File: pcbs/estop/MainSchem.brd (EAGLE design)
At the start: 99 x 99.5 mm, 30 parts, among them J1 XT60-M, J2 XT60-M, J3 XT60-M, J4 XT60-M, J5 XT60-M, Q1 FDBL9401-F085, Q2 FDBL9401-F085, U1 FAN3100T, U2 FAN3100T

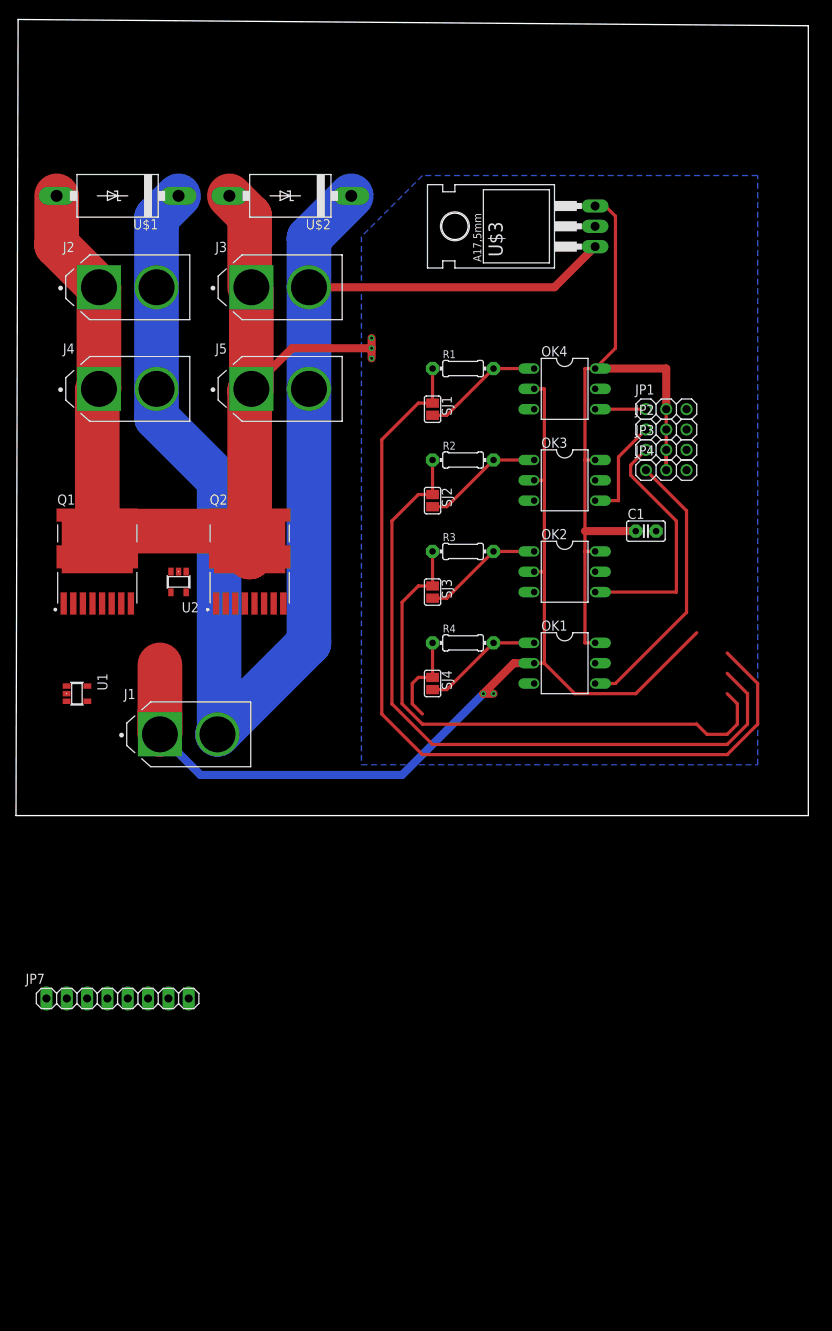
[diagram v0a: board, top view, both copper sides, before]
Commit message: Made improvements to e-stop layout and schematic. Added high-current pads.
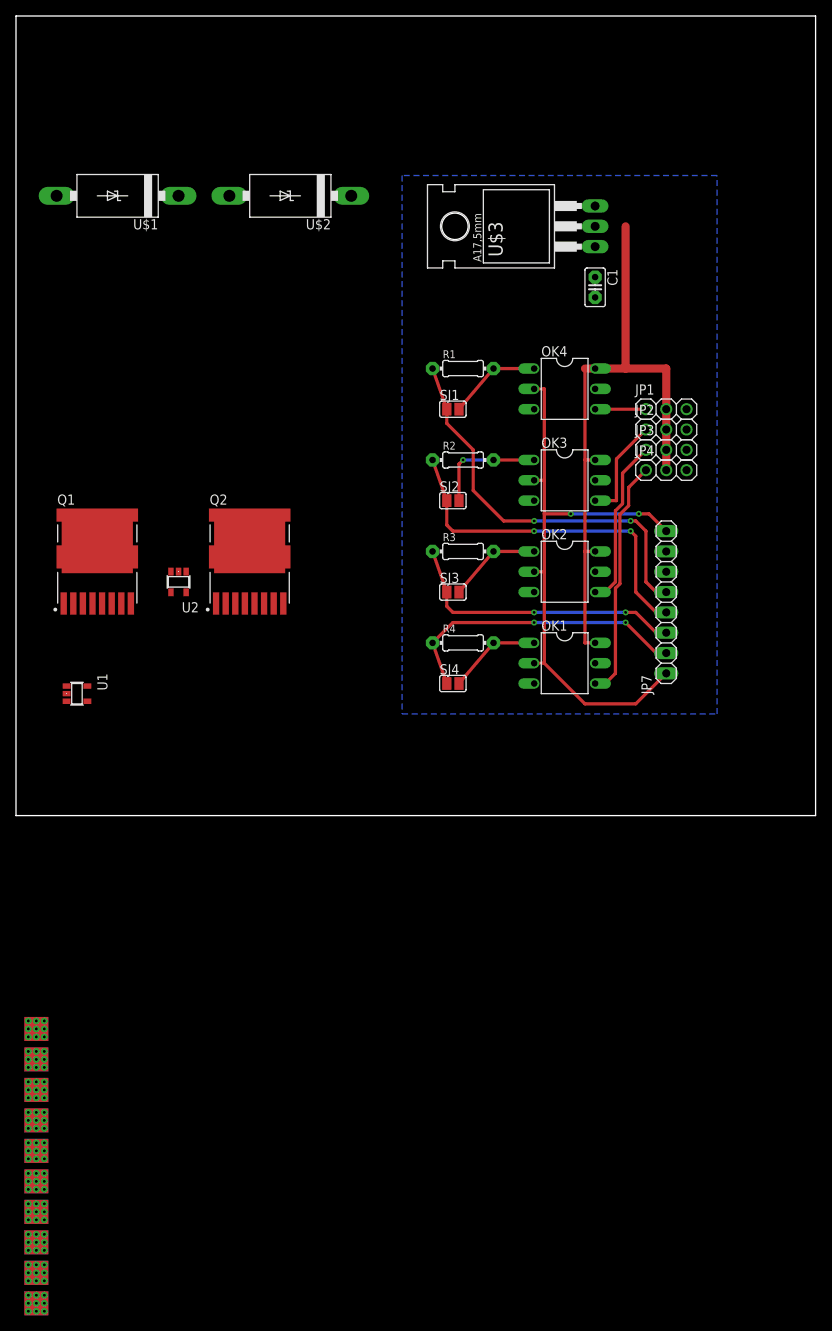
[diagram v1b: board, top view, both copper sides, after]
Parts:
- removed J1, J2, J3, J4, J5: XT60-M, XT60-M:AMASS_XT60-M
- added U$10, U$11, U$12, U$13, U$4, U$5, U$6, U$7, U$8, U$9: HIGH_CURRENT_WIRE_PAD, HighCurrentTransistorAndDriver:HIGH_CURRENT_WIRE_PAD
- moved JP7 84.6 mm to (81.3, 26.7), turned to 90 degrees
- moved C1 31.1 mm to (72.4, 66.0), turned to 270 degrees
- moved SJ1 2.54 mm to (54.6, 50.8), turned to 0 degrees
- moved SJ2 2.54 mm to (54.6, 39.4), turned to 0 degrees
- moved SJ3 2.54 mm to (54.6, 27.9), turned to 0 degrees
- moved SJ4 2.54 mm to (54.6, 16.5), turned to 0 degrees
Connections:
- net N$8 renamed ESTOP_LOW
- removed net BAT+: J1.2, J2.2, J3.2, J4.2, J5.2, JP7.7, U$1.C, U$2.C, U$3.1, U1.1, U2.1
- removed net ESC_GND: C1.2, J2.1, J3.1, J4.1, J5.1, JP1.3, JP2.3, JP3.3, JP4.3, OK1.5, OK2.5, OK3.5, OK4.5, Q1.9_1, Q1.9_2, Q1.9_3, Q1.9_4, Q2.9_1, Q2.9_2, Q2.9_3, Q2.9_4, U$1.A, U$2.A, U$3.2
- removed net ESC_SIDE_5V: C1.1, JP1.2, JP2.2, JP3.2, JP4.2, OK1.6, OK2.6, OK3.6, OK4.6, U$3.3
- removed net TRUE_GND_BATT-: J1.1, JP7.1, JP7.8, OK1.2, OK2.2, OK3.2, OK4.2, Q1.2, Q1.3, Q1.4, Q1.5, Q1.6, Q1.7, Q1.8, Q2.2, Q2.3, Q2.4, Q2.5, Q2.6, Q2.7, Q2.8, U1.2, U1.4, U2.2, U2.4
- new net +V: C1.1, JP1.2, JP2.2, JP3.2, JP4.2, JP7.7, OK1.6, OK2.6, OK3.6, OK4.6, U$1.C, U$10.P$1, U$10.P$2, U$10.P$3, U$10.P$4, U$10.P$5, U$10.P$6, U$10.P$7, U$10.P$8, U$10.P$9, U$12.P$1, U$12.P$2, U$12.P$3, U$12.P$4, U$12.P$5, U$12.P$6, U$12.P$7, U$12.P$8, U$12.P$9, U$2.C, U$3.1, U$3.3, U$4.P$1, U$4.P$2, U$4.P$3, U$4.P$4, U$4.P$5, U$4.P$6, U$4.P$7, U$4.P$8, U$4.P$9, U$6.P$1, U$6.P$2, U$6.P$3, U$6.P$4, U$6.P$5, U$6.P$6, U$6.P$7, U$6.P$8, U$6.P$9, U$8.P$1, U$8.P$2, U$8.P$3, U$8.P$4, U$8.P$5, U$8.P$6, U$8.P$7, U$8.P$8, U$8.P$9, U1.1, U2.1
- new net EGND: JP7.1, JP7.8, OK1.2, OK2.2, OK3.2, OK4.2, Q1.2, Q1.3, Q1.4, Q1.5, Q1.6, Q1.7, Q1.8, Q2.2, Q2.3, Q2.4, Q2.5, Q2.6, Q2.7, Q2.8, U$13.P$1, U$13.P$2, U$13.P$3, U$13.P$4, U$13.P$5, U$13.P$6, U$13.P$7, U$13.P$8, U$13.P$9, U1.2, U1.4, U2.2, U2.4
- new net VSS: C1.2, JP1.3, JP2.3, JP3.3, JP4.3, OK1.5, OK2.5, OK3.5, OK4.5, Q1.9_1, Q1.9_2, Q1.9_3, Q1.9_4, Q2.9_1, Q2.9_2, Q2.9_3, Q2.9_4, U$1.A, U$11.P$1, U$11.P$2, U$11.P$3, U$11.P$4, U$11.P$5, U$11.P$6, U$11.P$7, U$11.P$8, U$11.P$9, U$2.A, U$3.2, U$5.P$1, U$5.P$2, U$5.P$3, U$5.P$4, U$5.P$5, U$5.P$6, U$5.P$7, U$5.P$8, U$5.P$9, U$7.P$1, U$7.P$2, U$7.P$3, U$7.P$4, U$7.P$5, U$7.P$6, U$7.P$7, U$7.P$8, U$7.P$9, U$9.P$1, U$9.P$2, U$9.P$3, U$9.P$4, U$9.P$5, U$9.P$6, U$9.P$7, U$9.P$8, U$9.P$9
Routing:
- net BAT+: track 185.2 -> 0.00 mm
- net ESC_GND: track 141.0 -> 0.00 mm, vias 3 -> 0
- net TRUE_GND_BATT-: track 130.5 -> 0.00 mm, vias 2 -> 0
- net ESC_SIDE_5V: track 93.0 -> 0.00 mm
- net +V: track 0.00 -> 78.7 mm
- net EGND: track 0.00 -> 74.4 mm, vias 0 -> 2
- net N$20: track 108.0 -> 50.0 mm, vias 0 -> 2
- net N$18: track 88.6 -> 44.5 mm, vias 0 -> 2
- net N$15: track 70.0 -> 36.0 mm, vias 0 -> 2
- net N$10: track 11.5 -> 37.2 mm, vias 0 -> 2
- net N$11: track 31.1 -> 21.2 mm
- net N$9: track 35.0 -> 30.0 mm
- net N$5: track 15.1 -> 11.7 mm
- net N$16: track 15.1 -> 11.7 mm
- net N$19: track 15.1 -> 11.7 mm
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- added copper zone on layer 16, net VSS
- removed copper zone on layer 16, net ESC_GND
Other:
- board size 99 x 99.5 mm -> 99.9 x 99.9 mm

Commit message: E-stop board layout appears complete.
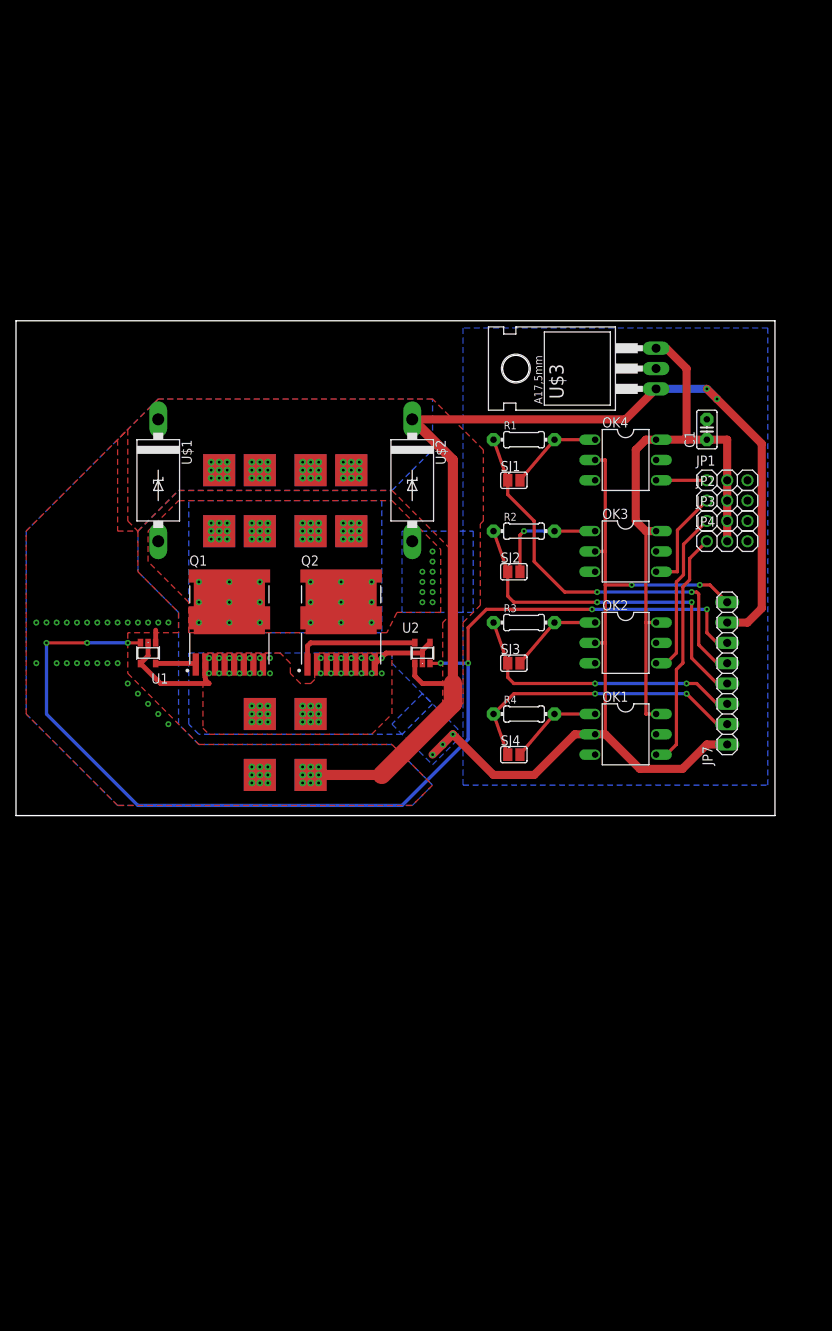
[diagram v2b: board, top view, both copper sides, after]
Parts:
- added U$14, U$15: HIGH_CURRENT_WIRE_PAD, HighCurrentTransistorAndDriver:HIGH_CURRENT_WIRE_PAD
- moved U$10 98.8 mm to (36.8, 43.2), flipped to the bottom, turned to 270 degrees
- moved U$11 97.2 mm to (41.9, 35.6), flipped to the bottom, turned to 270 degrees
- moved U$8 88.1 mm to (25.4, 43.2), flipped to the bottom, turned to 270 degrees
- moved U$9 85.9 mm to (30.5, 35.6), flipped to the bottom, turned to 270 degrees
- moved U$6 82.4 mm to (30.5, 43.2)
- moved U$4 80.2 mm to (41.9, 43.2)
- moved U$13 78.8 mm to (30.5, 12.7), flipped to the bottom, turned to 270 degrees
- moved U$7 77.1 mm to (25.4, 35.6), flipped to the bottom, turned to 270 degrees
- moved U$5 74.4 mm to (36.8, 35.6)
- moved U$12 68.2 mm to (30.5, 5.08), flipped to the bottom, turned to 270 degrees
- moved U$2 38.7 mm to (49.5, 41.9), turned to 270 degrees
- moved U$1 35.9 mm to (17.8, 41.9), turned to 270 degrees
- moved U2 31.8 mm to (50.8, 20.3), turned to 0 degrees
- moved C1 22.6 mm to (86.4, 48.3), turned to 90 degrees
- moved U$3 19.3 mm to (73.7, 55.9)
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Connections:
- removed net +V: C1.1, JP1.2, JP2.2, JP3.2, JP4.2, JP7.7, OK1.6, OK2.6, OK3.6, OK4.6, U$1.C, U$10.P$1, U$10.P$2, U$10.P$3, U$10.P$4, U$10.P$5, U$10.P$6, U$10.P$7, U$10.P$8, U$10.P$9, U$12.P$1, U$12.P$2, U$12.P$3, U$12.P$4, U$12.P$5, U$12.P$6, U$12.P$7, U$12.P$8, U$12.P$9, U$2.C, U$3.1, U$3.3, U$4.P$1, U$4.P$2, U$4.P$3, U$4.P$4, U$4.P$5, U$4.P$6, U$4.P$7, U$4.P$8, U$4.P$9, U$6.P$1, U$6.P$2, U$6.P$3, U$6.P$4, U$6.P$5, U$6.P$6, U$6.P$7, U$6.P$8, U$6.P$9, U$8.P$1, U$8.P$2, U$8.P$3, U$8.P$4, U$8.P$5, U$8.P$6, U$8.P$7, U$8.P$8, U$8.P$9, U1.1, U2.1
- new net +5V: C1.1, JP1.2, JP2.2, JP3.2, JP4.2, OK1.6, OK2.6, OK3.6, OK4.6, U$3.3
- new net V+: JP7.7, U$1.C, U$10.P$1, U$10.P$2, U$10.P$3, U$10.P$4, U$10.P$5, U$10.P$6, U$10.P$7, U$10.P$8, U$10.P$9, U$12.P$1, U$12.P$2, U$12.P$3, U$12.P$4, U$12.P$5, U$12.P$6, U$12.P$7, U$12.P$8, U$12.P$9, U$15.P$1, U$15.P$2, U$15.P$3, U$15.P$4, U$15.P$5, U$15.P$6, U$15.P$7, U$15.P$8, U$15.P$9, U$2.C, U$3.1, U$4.P$1, U$4.P$2, U$4.P$3, U$4.P$4, U$4.P$5, U$4.P$6, U$4.P$7, U$4.P$8, U$4.P$9, U$6.P$1, U$6.P$2, U$6.P$3, U$6.P$4, U$6.P$5, U$6.P$6, U$6.P$7, U$6.P$8, U$6.P$9, U$8.P$1, U$8.P$2, U$8.P$3, U$8.P$4, U$8.P$5, U$8.P$6, U$8.P$7, U$8.P$8, U$8.P$9, U1.1, U2.1
- net EGND: now also U$14.P$1, U$14.P$2, U$14.P$3, U$14.P$4, U$14.P$5, U$14.P$6, U$14.P$7, U$14.P$8, U$14.P$9
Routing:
- net V+: track 0.00 -> 143.0 mm, vias 0 -> 29
- net ESTOP_LOW: track 0.00 -> 137.0 mm, vias 0 -> 7
- net +V: track 78.7 -> 0.00 mm
- net +5V: track 0.00 -> 75.8 mm
- net EGND: track 74.4 -> 124.1 mm, vias 2 -> 33
- net N$4: track 0.00 -> 15.9 mm
- net N$6: track 0.00 -> 5.06 mm
- added copper zone on layer 1, net EGND
- added copper zone on layer 16, net EGND
- added copper zone on layer 1, net V+
- added copper zone on layer 16, net V+
- added copper zone on layer 1, net VSS
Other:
- board size 99.9 x 99.9 mm -> 94.9 x 61.8 mm

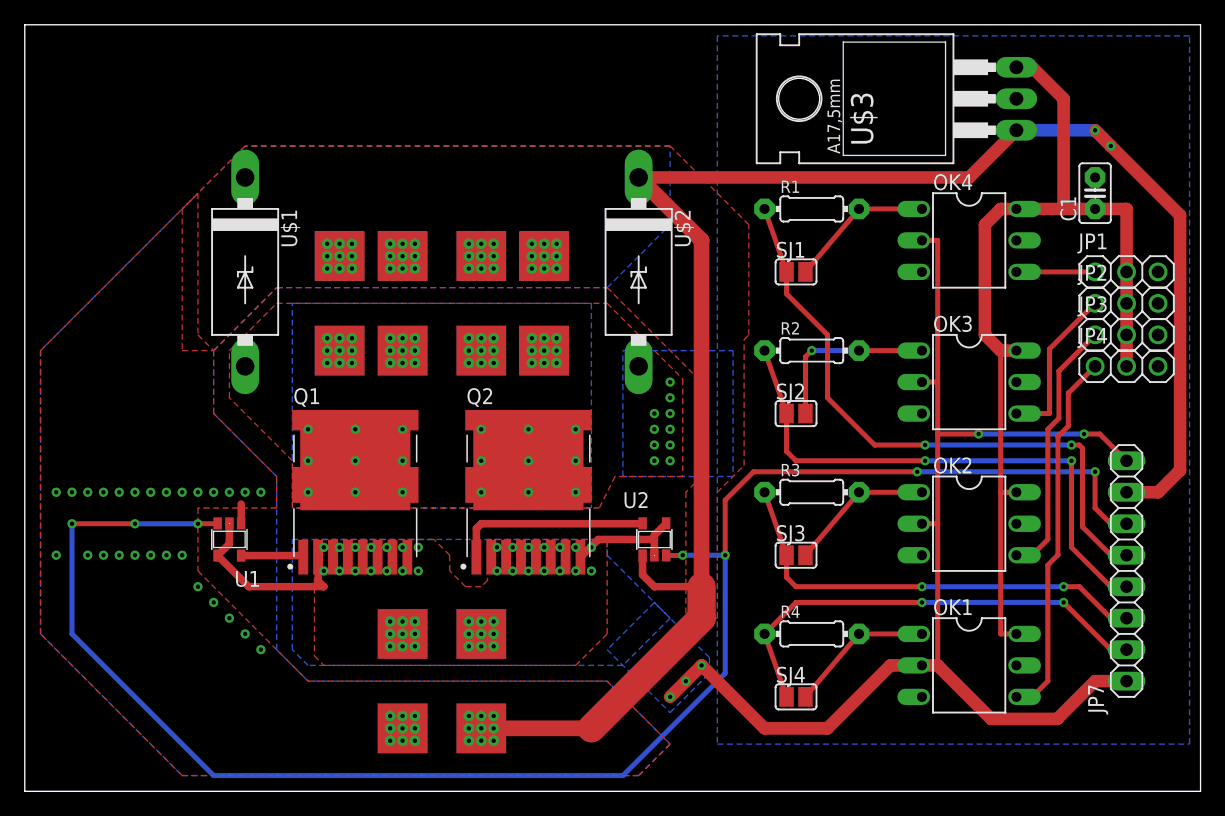
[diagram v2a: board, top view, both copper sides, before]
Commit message: Imported RPi mounting holes from one of my previous projects. Added RPi-compatible mounting holes to E-stop board.
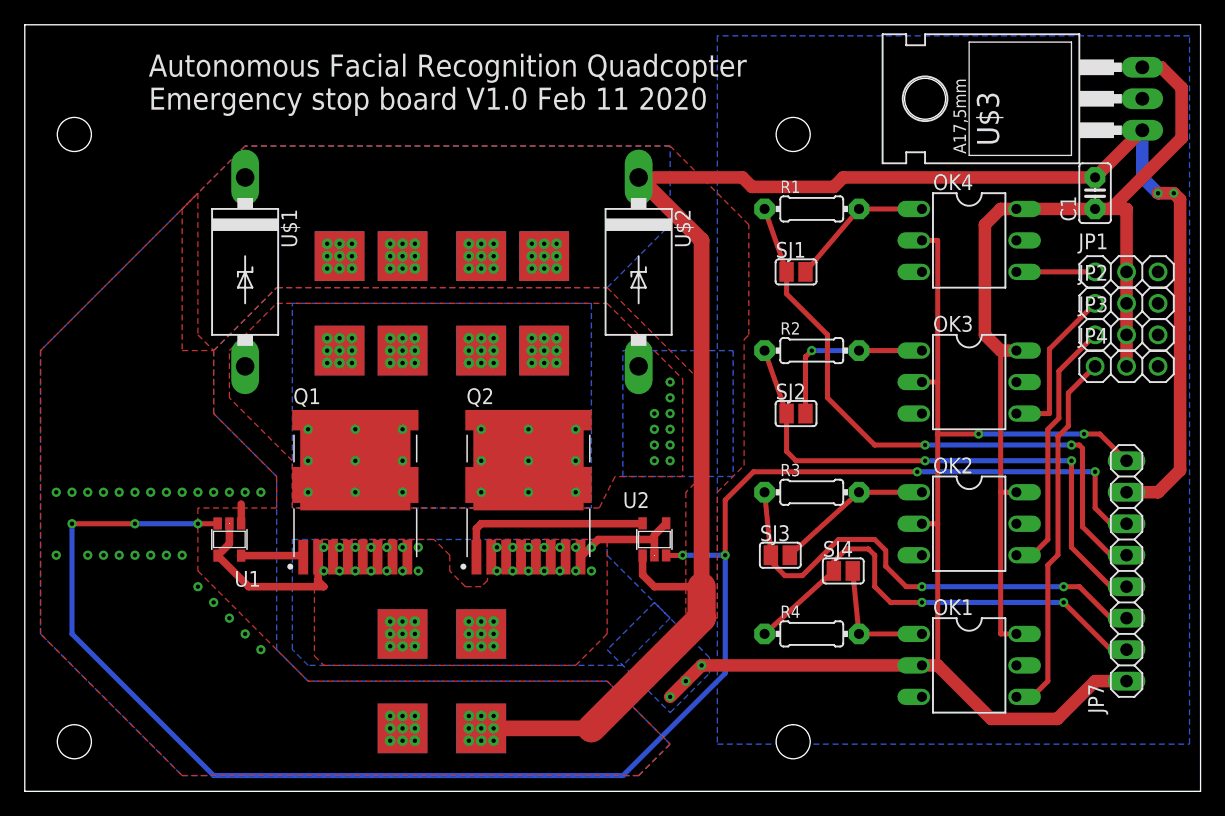
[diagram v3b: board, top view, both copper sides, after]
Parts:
- added U$16, U$17, U$18, U$19: (no value), HighCurrentTransistorAndDriver:RPI_MOUNTING_HOLE
- moved SJ4 10.9 mm to (66.0, 17.8)
- moved U$3 10.2 mm to (83.8, 55.9)
- moved SJ3 1.27 mm to (61.0, 19.1)
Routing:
- net EGND: track 124.1 -> 119.9 mm
- net N$15: track 36.0 -> 39.4 mm
- net V+: track 143.0 -> 146.0 mm
- net +5V: track 75.8 -> 78.0 mm
- net N$5: track 11.7 -> 10.2 mm
- net N$16: track 11.7 -> 12.6 mm
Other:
- board text added: "Autonomous Facial Recognition Quadcopter Emergency stop board V1.0 Feb 11 2020"
